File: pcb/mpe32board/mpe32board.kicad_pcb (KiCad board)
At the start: 4 copper layers, 98 x 79 mm, 159 parts, among them J1 Conn_ST_STDC14, J10 Conn_01x04, J11 Conn_01x04, J12 Conn_01x04, J13 Conn_01x04, J14 Conn_01x04, J15 Conn_01x04, J16 Conn_01x04, J17 Conn_01x04, J18 Conn_01x04, J19 Conn_01x04, J2 USB_C_Receptacle_USB2.0_16P, J20 Conn_01x04, J21 Conn_01x04, J22 Conn_01x04, J23 Conn_01x04, J24 Conn_01x04, J25 Conn_01x04, J26 Conn_01x04, J27 Conn_01x04, J3 Conn_01x01_Socket, J4 Conn_01x04, J44 Conn_01x05, J45 Conn_01x04_Socket, J46 Conn_02x10_Counter_Clockwise, J48 Micro_SD_Card_Det_Hirose_DM3AT, J49 AudioJack3_SwitchT, J5 Conn_01x04, J6 Conn_01x04, J7 Conn_01x04, J8 Conn_01x04, J9 Conn_01x04, SW1 SW_Push, SW2 SW_Push, SW3 SW_Push, SW4 SW_Push, SW5 SW_Push, SW6 SW_Push, U1 TAC5212IRGER, U10 W9812G6KH-75, U11 IP4252CZ16, U2 USBLC6-2P6, U3 AMS1117-3.3, U4 TCA9548ARGER, U5 TCA9548ARGER, U6 TCA9548ARGER, U9 STM32H743IITx

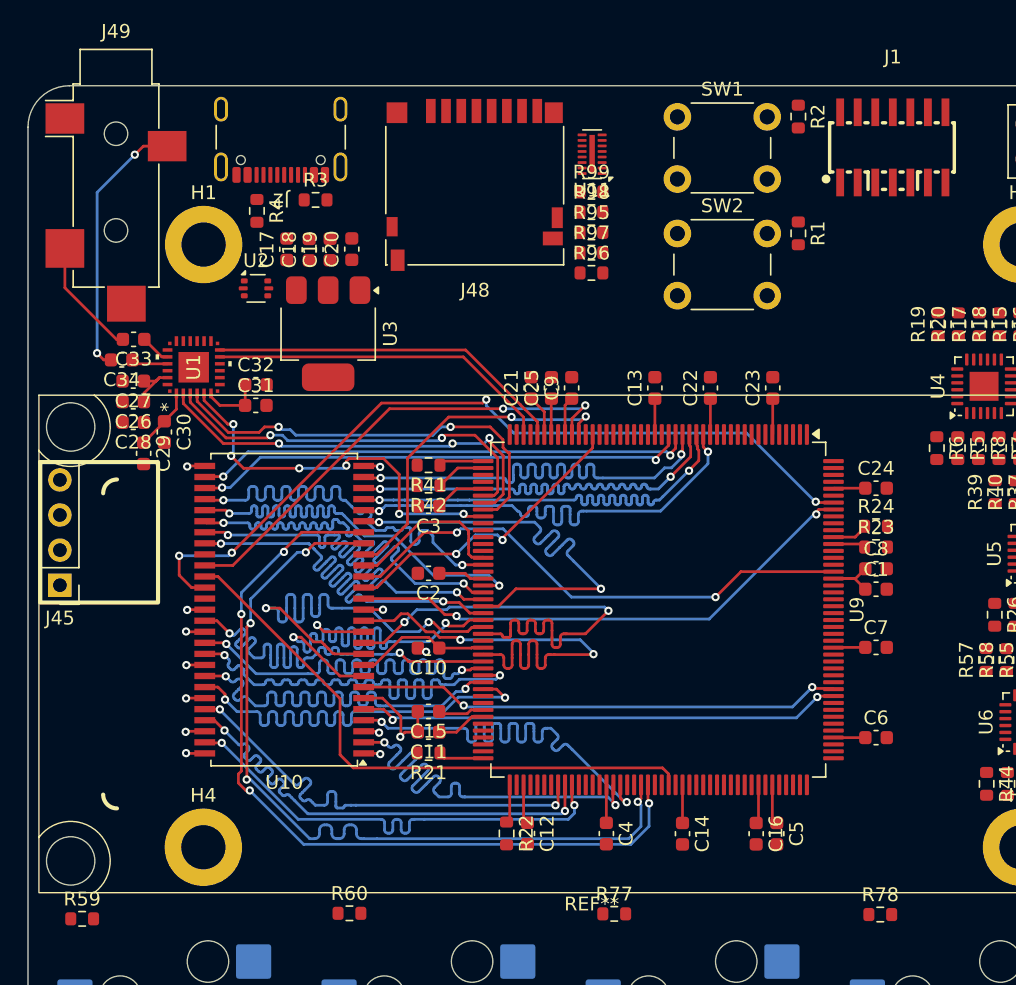
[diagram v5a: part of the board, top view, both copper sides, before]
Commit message: routed audio codec and sdram
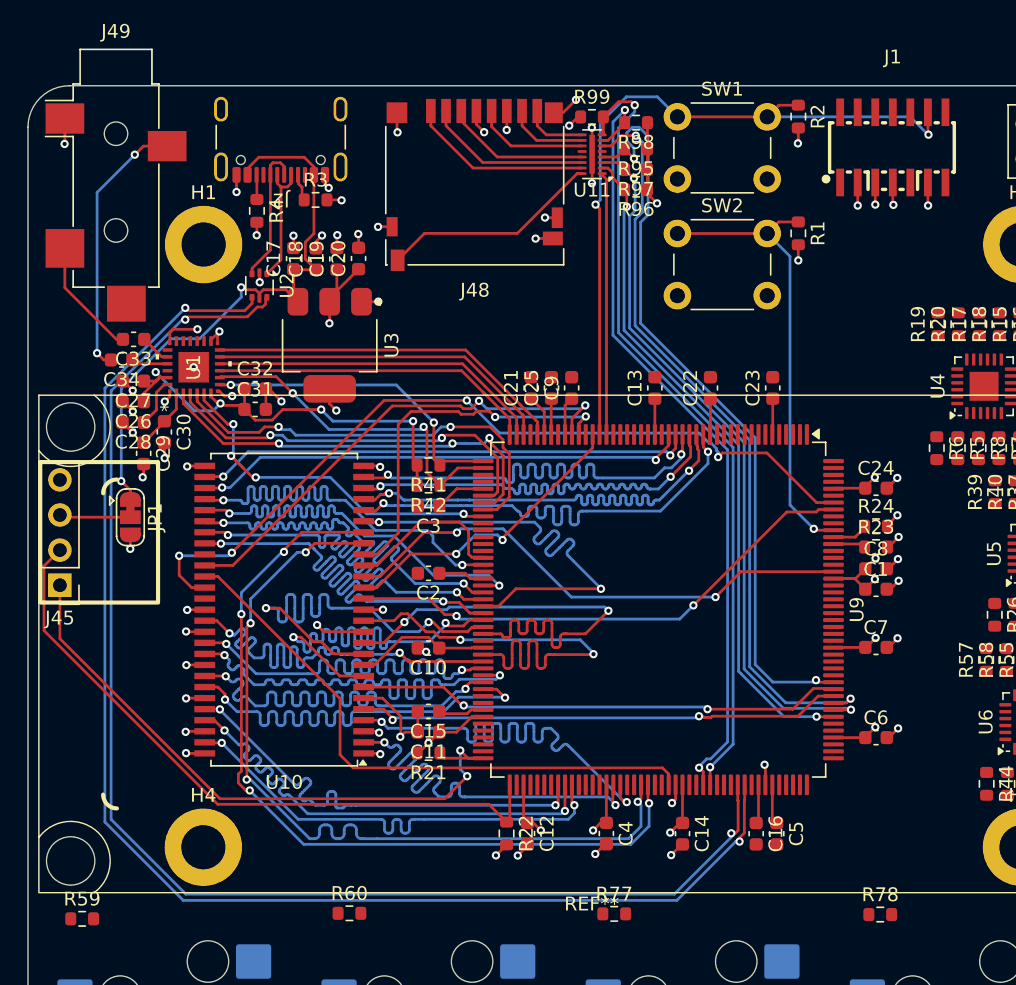
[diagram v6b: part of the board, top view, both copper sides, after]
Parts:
- added JP1: SolderJumper_3_Bridged12, Jumper:SolderJumper-3_P1.3mm_Bridged12_RoundedPad1.0x1.5mm, F.Cu at (67.4, 111.2)
- moved R98 7.24 mm to (104.0, 82.7), turned to 180 degrees
- moved R95 6.85 mm to (104.0, 84.6), turned to 180 degrees
- moved R96 6.84 mm to (104.0, 87.5), turned to 180 degrees
- moved R97 6.83 mm to (104.0, 86.1), turned to 180 degrees
- moved R99 5.42 mm to (100.8, 82.3)
- moved U3 0.85 mm to (81.8, 98.8)
- moved C18 0.84 mm to (80.8, 92.5)
- moved C17 0.84 mm to (79.2, 92.5)
- moved C19 0.84 mm to (82.3, 92.5)
- moved C20 0.84 mm to (83.9, 92.5)
- moved U2 0.32 mm to (76.8, 94.5), turned to -90 degrees
- moved C31 0.29 mm to (76.4, 103.4)
- moved C32 0.29 mm to (76.4, 101.9)
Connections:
- net OTG_FS_DM renamed OTG_FS_DN
- J45 pad 3: +5V -> Net-(J45-Pin_3)
- U11 pad 17: unconnected-(U11-GND-Pad17) -> GND
- U9 pad 1: NEOPIXEL_INTERNAL -> unconnected-(U9-PE2-Pad1)
- U9 pad 133: unconnected-(U9-PI2-Pad133) -> NEOPIXEL_INTERNAL
- U9 pad 176: unconnected-(U9-PI7-Pad176) -> NEOPIXEL_IN
- U9 pad 30: unconnected-(U9-PH1-Pad30) -> SDCARD_DET
- U9 pad 41: SDCARD_DET -> unconnected-(U9-PA1-Pad41)
- U9 pad 43: unconnected-(U9-PH2-Pad43) -> TAC5212_GPIO2
- U9 pad 44: NEOPIXEL_IN -> TAC5212_GPIO1
- U9 pad 79: TAC5212_GPIO1 -> unconnected-(U9-PB10-Pad79)
- U9 pad 80: TAC5212_GPIO2 -> unconnected-(U9-PB11-Pad80)
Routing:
- net OTG_FS_DP: track 0.00 -> 99.6 mm, vias 0 -> 2
- net OTG_FS_DN: track 0.00 -> 98.3 mm, vias 0 -> 2
- net SDMMC1_D1: track 0.00 -> 57.9 mm, vias 0 -> 2
- net SDMMC1_D0: track 0.00 -> 56.9 mm, vias 0 -> 2
- net GND: track 18.6 -> 75.4 mm, vias 8 -> 52
- net SDMMC1_CMD: track 0.00 -> 55.1 mm, vias 0 -> 2
- net SDMMC1_CK: track 0.00 -> 54.9 mm, vias 0 -> 2
- net NRST: track 0.00 -> 52.7 mm, vias 0 -> 2
- net SDMMC1_D3: track 0.00 -> 52.2 mm, vias 0 -> 2
- net SDMMC1_D2: track 0.00 -> 49.1 mm, vias 0 -> 2
- net I2C4_SDA: track 2.78 -> 48.3 mm
- net +5V: track 0.00 -> 43.5 mm, vias 0 -> 2
- net I2C4_SCL: track 3.25 -> 46.0 mm, vias 0 -> 2
- net +3V3: track 67.8 -> 104.0 mm, vias 6 -> 26
- net BOOT0: track 0.00 -> 33.3 mm, vias 0 -> 1
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
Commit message: route connectors
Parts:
- moved J20 37.9 mm to (145.6, 155.8)
- moved J11 31.7 mm to (145.6, 103.0)
- moved J10 31.7 mm to (145.6, 97.7)
- moved J21 31.7 mm to (153.5, 155.8)
- moved J9 27.6 mm to (153.5, 97.7)
- moved J15 26.4 mm to (145.6, 129.4)
- moved J16 26.4 mm to (153.5, 124.1)
- moved J14 22.6 mm to (153.5, 129.4)
- moved J22 21.2 mm to (153.5, 150.6)
- moved J8 17.7 mm to (153.5, 103.0)
- moved J23 17.7 mm to (145.6, 150.6)
- moved J17 15.9 mm to (153.5, 118.8)
- moved J4 15.9 mm to (145.6, 113.5)
- moved J19 13.2 mm to (145.6, 124.1)
- moved J5 13.2 mm to (153.5, 113.5)
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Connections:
- U9 pad 100: unconnected-(U9-PD12-Pad100) -> BTN2_INTERNAL
- U9 pad 116: unconnected-(U9-PC7-Pad116) -> BTN3_INTERNAL
- U9 pad 119: unconnected-(U9-PA8-Pad119) -> BTN4_INTERNAL
- U9 pad 134: unconnected-(U9-PI3-Pad134) -> RESET_0
- U9 pad 145: BTN1_INTERNAL -> unconnected-(U9-PD3-Pad145)
- U9 pad 146: BTN2_INTERNAL -> unconnected-(U9-PD4-Pad146)
- U9 pad 147: BTN3_INTERNAL -> unconnected-(U9-PD5-Pad147)
- U9 pad 150: BTN4_INTERNAL -> unconnected-(U9-PD6-Pad150)
- U9 pad 99: unconnected-(U9-PD11-Pad99) -> BTN1_INTERNAL
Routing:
- net +3V3: track 104.0 -> 331.2 mm, vias 26 -> 62
- net GND: track 75.4 -> 278.6 mm, vias 52 -> 91
- net I2C1_SDA: track 2.54 -> 86.5 mm, vias 0 -> 4
- net RESET_0: track 0.00 -> 77.4 mm, vias 0 -> 4
- net I2C1_SCL: track 2.39 -> 77.3 mm, vias 0 -> 4
- net LPUART1_RX: track 0.00 -> 64.1 mm, vias 0 -> 2
- net LPUART1_TX: track 0.00 -> 59.2 mm, vias 0 -> 2
- net SWDIO: track 0.00 -> 57.6 mm, vias 0 -> 2
- net BTN1_INTERNAL: track 0.00 -> 49.9 mm, vias 0 -> 1
- net SWCLK: track 0.00 -> 49.4 mm, vias 0 -> 2
- net NEOPIXEL_IN: track 0.00 -> 49.0 mm, vias 0 -> 3
- net JTDI: track 0.00 -> 48.9 mm, vias 0 -> 2
- net 17_SD1: track 0.00 -> 42.7 mm, vias 0 -> 2
- net 17_SC1: track 0.00 -> 42.3 mm, vias 0 -> 2
- net 16_SD0: track 0.00 -> 41.3 mm, vias 0 -> 2
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
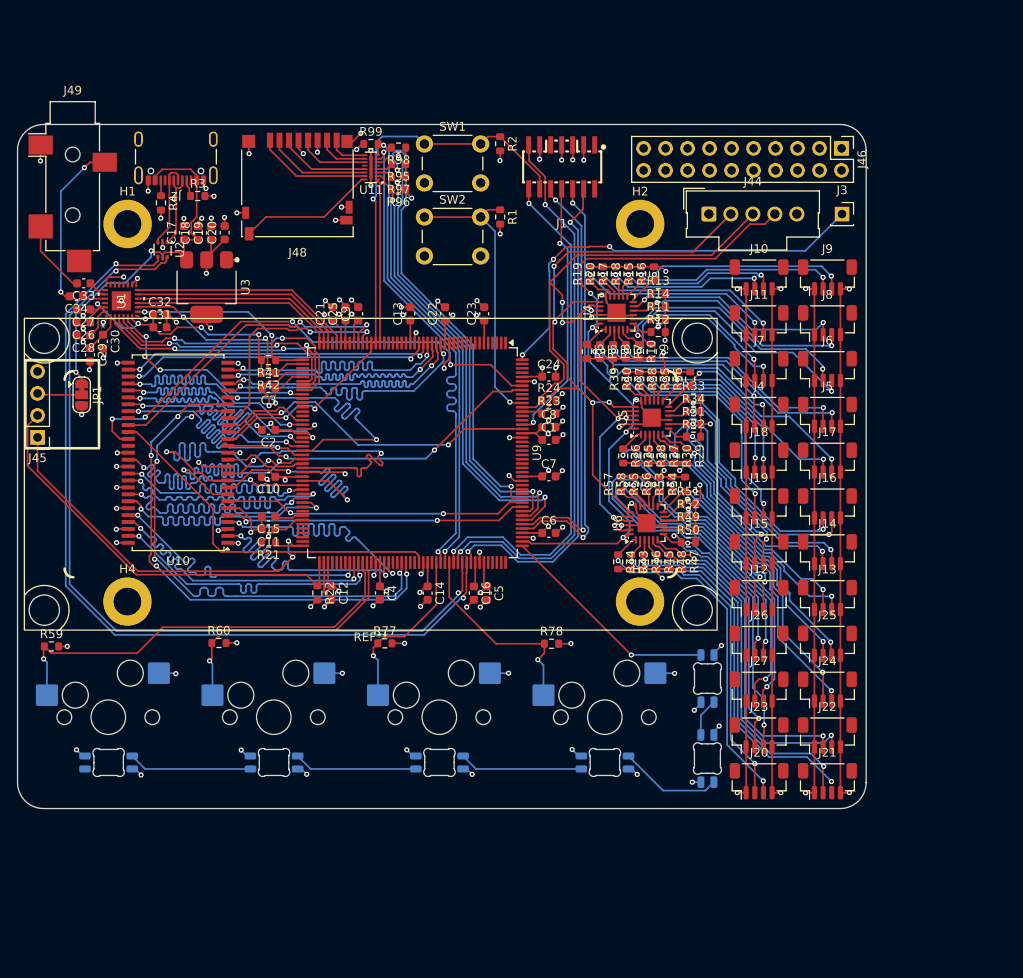
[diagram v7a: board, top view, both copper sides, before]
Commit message: finish hacker header routing, drc checked
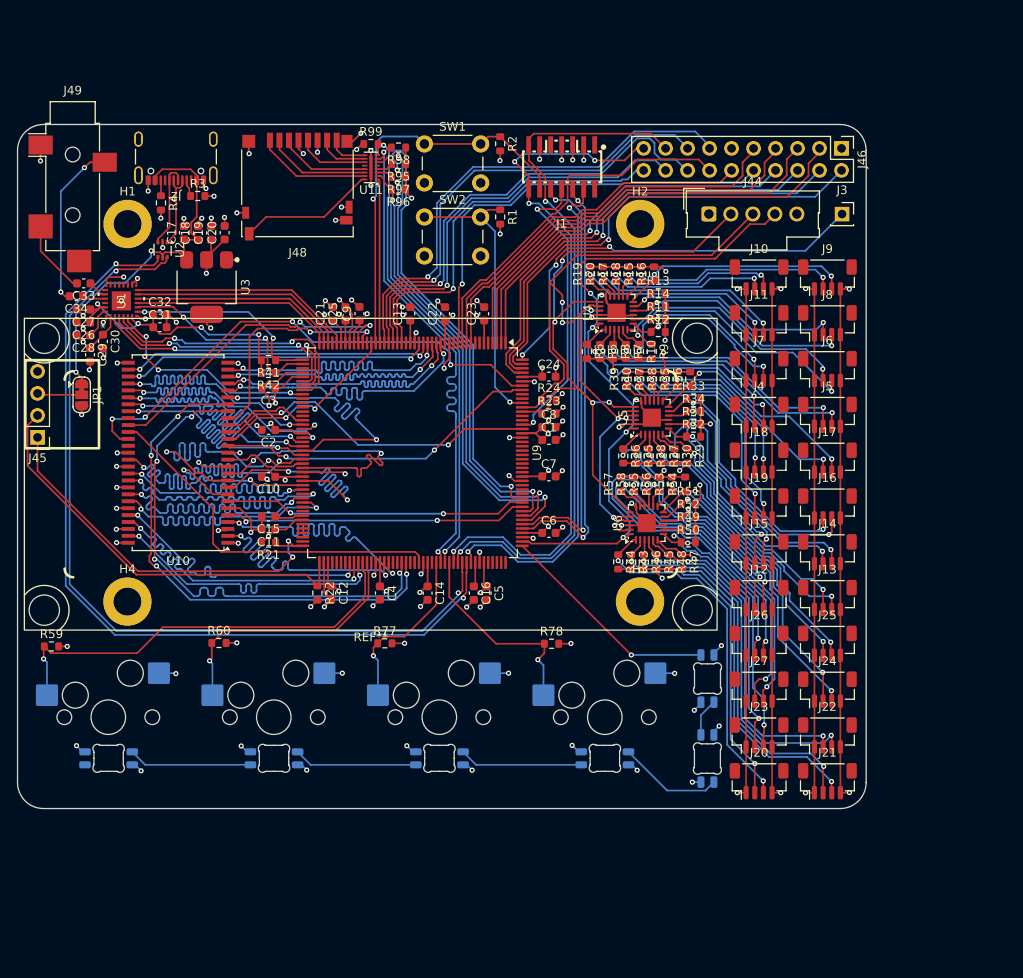
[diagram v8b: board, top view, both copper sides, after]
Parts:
- moved D4 0.48 mm to (127.8, 153.2)
- moved D5 0.48 mm to (108.7, 153.2)
- moved D6 0.48 mm to (89.6, 153.2)
- moved D7 0.48 mm to (70.5, 153.2)
- moved C9 0.15 mm to (99.5, 101.8)
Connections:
- J46 pad 1: unconnected-(J46-Pin_1-Pad1) -> +3V3
- J46 pad 10: unconnected-(J46-Pin_10-Pad10) -> GPIO_PI10
- J46 pad 11: unconnected-(J46-Pin_11-Pad11) -> GND
- J46 pad 12: unconnected-(J46-Pin_12-Pad12) -> GPIO_PC15
- J46 pad 13: unconnected-(J46-Pin_13-Pad13) -> GPIO_PH0
- J46 pad 14: unconnected-(J46-Pin_14-Pad14) -> GPIO_PI9
- J46 pad 15: unconnected-(J46-Pin_15-Pad15) -> GPIO_PF10
- J46 pad 16: unconnected-(J46-Pin_16-Pad16) -> GPIO_PF9
- J46 pad 17: unconnected-(J46-Pin_17-Pad17) -> LPUART1_RX
- J46 pad 18: unconnected-(J46-Pin_18-Pad18) -> GPIO_PF8
- J46 pad 19: unconnected-(J46-Pin_19-Pad19) -> LPUART1_TX
- J46 pad 2: unconnected-(J46-Pin_2-Pad2) -> GPIO_PI6
- J46 pad 20: unconnected-(J46-Pin_20-Pad20) -> GPIO_PF7
- J46 pad 3: unconnected-(J46-Pin_3-Pad3) -> GPIO_PE3
- J46 pad 4: unconnected-(J46-Pin_4-Pad4) -> GPIO_PI5
- J46 pad 5: unconnected-(J46-Pin_5-Pad5) -> GPIO_PE4
- J46 pad 6: unconnected-(J46-Pin_6-Pad6) -> GPIO_PI4
- J46 pad 7: unconnected-(J46-Pin_7-Pad7) -> GPIO_PE5
- J46 pad 8: unconnected-(J46-Pin_8-Pad8) -> GPIO_PE2
- J46 pad 9: unconnected-(J46-Pin_9-Pad9) -> GPIO_PC14
- U9 pad 1: unconnected-(U9-PE2-Pad1) -> GPIO_PE2
- U9 pad 10: unconnected-(U9-PC15-Pad10) -> GPIO_PC15
- U9 pad 11: unconnected-(U9-PI9-Pad11) -> GPIO_PI9
- U9 pad 12: unconnected-(U9-PI10-Pad12) -> GPIO_PI10
- U9 pad 173: unconnected-(U9-PI4-Pad173) -> GPIO_PI4
- U9 pad 174: unconnected-(U9-PI5-Pad174) -> GPIO_PI5
- U9 pad 175: unconnected-(U9-PI6-Pad175) -> GPIO_PI6
- U9 pad 2: unconnected-(U9-PE3-Pad2) -> GPIO_PE3
- U9 pad 25: unconnected-(U9-PF7-Pad25) -> GPIO_PF7
- U9 pad 26: unconnected-(U9-PF8-Pad26) -> GPIO_PF8
- U9 pad 27: unconnected-(U9-PF9-Pad27) -> GPIO_PF9
- U9 pad 28: unconnected-(U9-PF10-Pad28) -> GPIO_PF10
- U9 pad 29: unconnected-(U9-PH0-Pad29) -> GPIO_PH0
- U9 pad 3: unconnected-(U9-PE4-Pad3) -> GPIO_PE4
- U9 pad 4: unconnected-(U9-PE5-Pad4) -> GPIO_PE5
- U9 pad 9: unconnected-(U9-PC14-Pad9) -> GPIO_PC14
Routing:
- net GPIO_PH0: track 0.00 -> 56.5 mm, vias 0 -> 1
- net GPIO_PI6: track 0.00 -> 54.1 mm, vias 0 -> 1
- net GPIO_PF9: track 0.00 -> 53.6 mm, vias 0 -> 1
- net GPIO_PF10: track 0.00 -> 53.3 mm, vias 0 -> 1
- net GPIO_PI5: track 0.00 -> 52.4 mm, vias 0 -> 1
- net GPIO_PE3: track 0.00 -> 50.8 mm
- net GPIO_PI4: track 0.00 -> 50.7 mm, vias 0 -> 1
- net GPIO_PI10: track 0.00 -> 50.6 mm, vias 0 -> 1
- net GPIO_PE4: track 0.00 -> 48.8 mm
- net GPIO_PF8: track 0.00 -> 48.1 mm, vias 0 -> 1
- net GPIO_PE5: track 0.00 -> 46.8 mm
- net GPIO_PC14: track 0.00 -> 46.0 mm
- net GPIO_PF7: track 0.00 -> 44.4 mm, vias 0 -> 1
- net GPIO_PE2: track 0.00 -> 43.7 mm, vias 0 -> 1
- net GPIO_PI9: track 0.00 -> 42.5 mm
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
